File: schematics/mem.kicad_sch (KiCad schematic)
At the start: 6 parts, among them SW2 SW_DIP_x03, U8 SST39SF010A-70-4C-PHE, U9 AS7C256C-15PCN

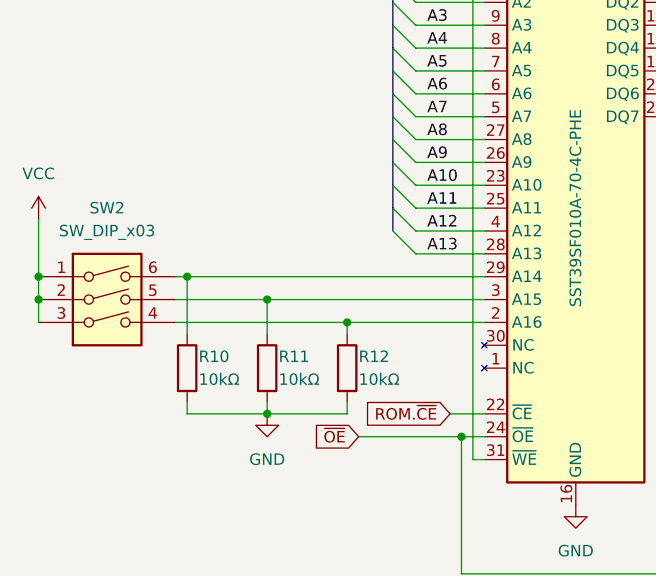
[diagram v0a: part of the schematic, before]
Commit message: Address decoder pld file and no-VIA keyboard schematic and pld file.
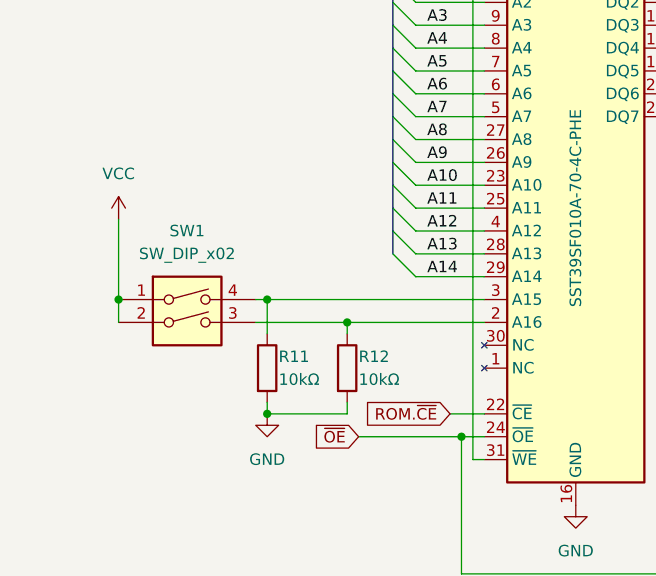
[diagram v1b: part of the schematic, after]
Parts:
- removed R10: 10kΩ, symbol Device:R
- removed SW2: SW_DIP_x03, symbol Switch:SW_DIP_x03
- added SW1: SW_DIP_x02, symbol Switch:SW_DIP_x02
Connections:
- net A14: now also U8.29 (A14)
- net VCC: now also SW1.1, SW1.2
- net at R12.1, U8.2 (A16): now also SW1.3
- net at R11.1, U8.3 (A15): now also SW1.4

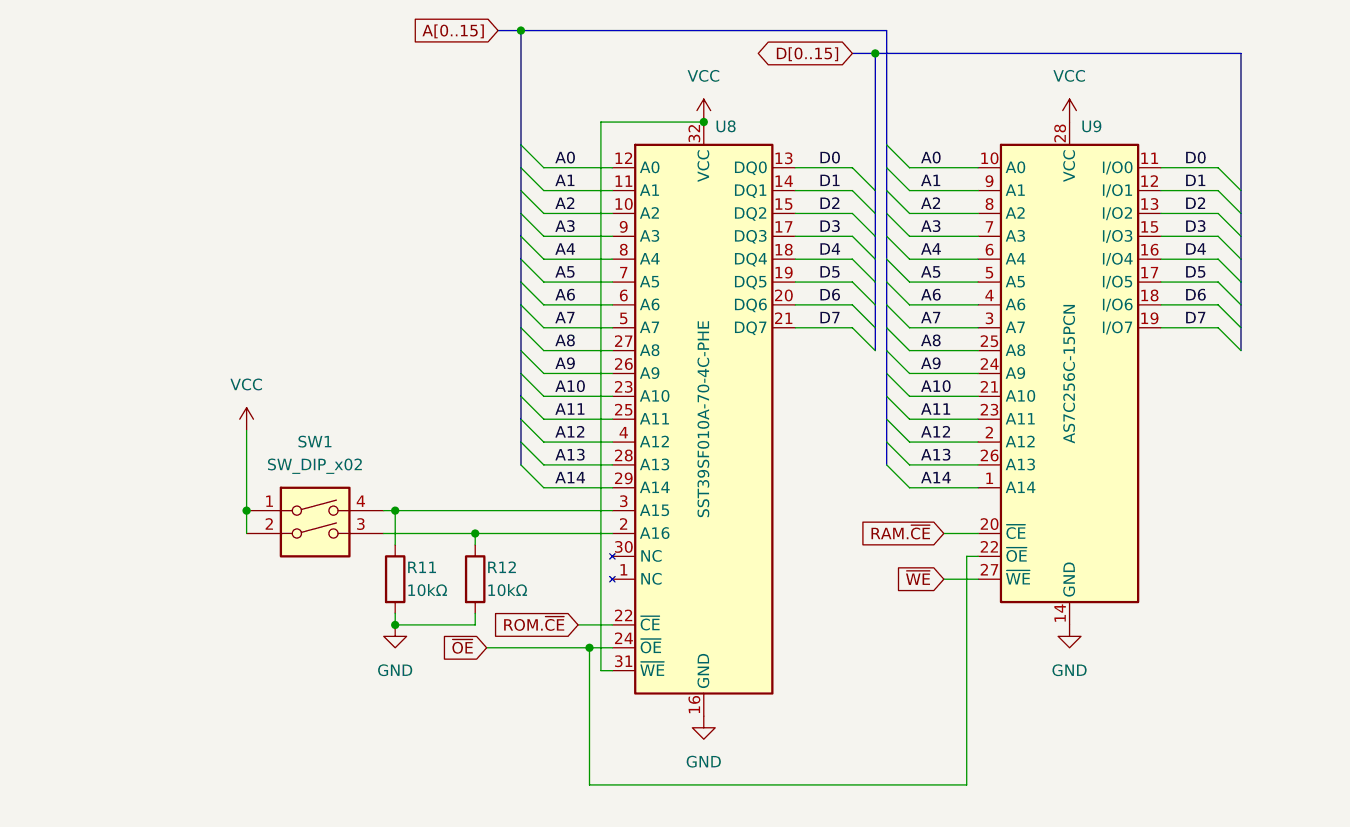
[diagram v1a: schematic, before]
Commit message: PLD files and schematics for address decoder, device selector, keyboard controller, lcd controller, banked memory, and bootloader.
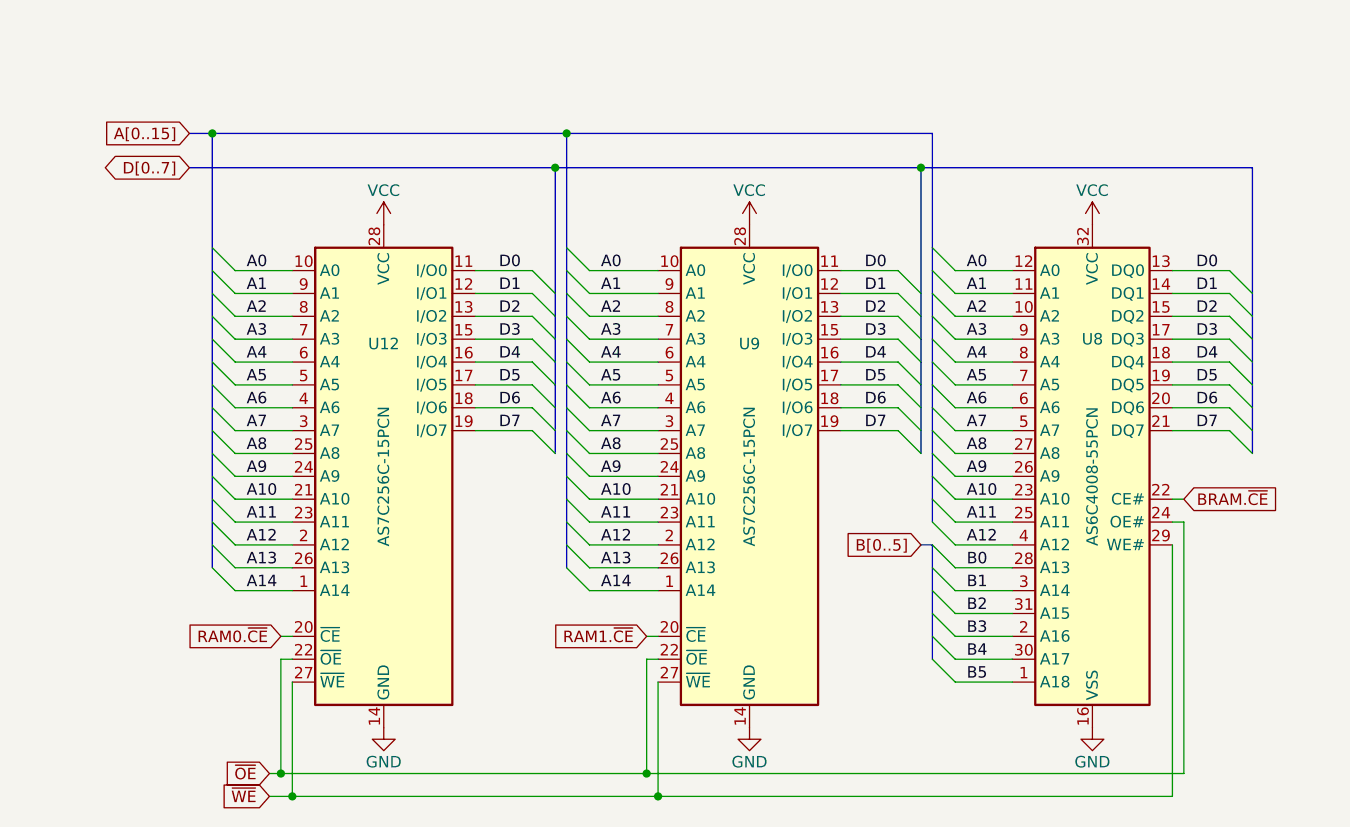
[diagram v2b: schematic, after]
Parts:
- removed R11, R12: 10kΩ, symbol Device:R
- removed SW1: SW_DIP_x02, symbol Switch:SW_DIP_x02
- removed U8: SST39SF010A-70-4C-PHE, symbol Memory_Flash:SST39SF010
- added U12: AS7C256C-15PCN, Package_DIP:DIP-28_W7.62mm, symbol Memory_RAM:KM62256CLP
- added U8: AS6C4008-55PCN, Package_DIP:DIP-32_W15.24mm, symbol Memory_RAM:AS6C4008-55PCN
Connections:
- net A0: now also U12.10 (A0), U8.12 (A0)
- net A1: now also U12.9 (A1), U8.11 (A1)
- net A10: now also U12.21 (A10), U8.23 (A10)
- net A11: now also U12.23 (A11), U8.25 (A11)
- net A12: now also U12.2 (A12), U8.4 (A12)
- net A13: now also U12.26 (A13)
- net A14: now also U12.1 (A14)
- net A2: now also U12.8 (A2), U8.10 (A2)
- net A3: now also U12.7 (A3), U8.9 (A3)
- net A4: now also U12.6 (A4), U8.8 (A4)
- net A5: now also U12.5 (A5), U8.7 (A5)
- net A6: now also U12.4 (A6), U8.6 (A6)
- net A7: now also U12.3 (A7), U8.5 (A7)
- net A8: now also U12.25 (A8), U8.27 (A8)
- net A9: now also U12.24 (A9), U8.26 (A9)
- net D0: now also U12.11 (I/O0), U8.13 (DQ0)
- net D1: now also U12.12 (I/O1), U8.14 (DQ1)
- net D2: now also U12.13 (I/O2), U8.15 (DQ2)
- net D3: now also U12.15 (I/O3), U8.17 (DQ3)
- net D4: now also U12.16 (I/O4), U8.18 (DQ4)
- net D5: now also U12.17 (I/O5), U8.19 (DQ5)
- net D6: now also U12.18 (I/O6), U8.20 (DQ6)
- net D7: now also U12.19 (I/O7), U8.21 (DQ7)
- net GND: now also U12.14 (GND), U8.16 (VSS)
- net VCC: now also U12.28 (VCC), U8.32 (VCC)
- net ~{OE}: now also U12.22 (~{OE}), U8.24 (OE#)
- net ~{WE}: now also U12.27 (~{WE}), U8.29 (WE#)
- net RAM.~{CE} renamed RAM1.~{CE}
- new net B0: U8.28 (A13)
- new net B1: U8.3 (A14)
- new net B2: U8.31 (A15)
- new net B3: U8.2 (A16)
- new net B4: U8.30 (A17)
- new net B5: U8.1 (A18)
- new net BRAM.~{CE}: U8.22 (CE#)
- new net RAM0.~{CE}: U12.20 (~{CE})
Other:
- moved on the sheet: U9

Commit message: updating schematics as I wire the board
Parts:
- renumbered U9 to U13, U8 to U14
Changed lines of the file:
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@@
 		(in_pos_files yes)
 		(dnp no)
-		(property "Reference" "#PWR019"
+		(property "Reference" "#PWR026"
 			(at 100.33 138.43 0)
 			(hide yes)
@@
 			(project "bv6502_hw"
 				(path "/94c72abe-aaa5-49aa-8ab7-5d3e7cbc10be/e0ef0165-61c4-4081-b725-ec037a3db6b2"
-					(reference "#PWR019")
+					(reference "#PWR026")
 					(unit 1)
 				)
@@
 		(in_pos_files yes)
 		(dnp no)
-		(property "Reference" "#PWR018"
+		(property "Reference" "#PWR025"
 			(at 100.33 80.01 0)
 			(hide yes)
@@
 			(project "bv6502_hw"
 				(path "/94c72abe-aaa5-49aa-8ab7-5d3e7cbc10be/e0ef0165-61c4-4081-b725-ec037a3db6b2"
-					(reference "#PWR018")
+					(reference "#PWR025")
 					(unit 1)
 				)
@@
 		(in_pos_files yes)
 		(dnp no)
-		(property "Reference" "U9"
+		(property "Reference" "U13"
 			(at 140.97 90.17 0)
 			(show_name no)
@@
 			(project "bv6502_hw"
 				(path "/94c72abe-aaa5-49aa-8ab7-5d3e7cbc10be/e0ef0165-61c4-4081-b725-ec037a3db6b2"
-					(reference "U9")
+					(reference "U13")
 					(unit 1)
 				)
@@
 		(dnp no)
 		(fields_autoplaced yes)
-		(property "Reference" "U8"
+		(property "Reference" "U14"
 			(at 179.07 88.9 0)
 			(show_name no)
@@
 			(project "bv6502_hw"
 				(path "/94c72abe-aaa5-49aa-8ab7-5d3e7cbc10be/e0ef0165-61c4-4081-b725-ec037a3db6b2"
-					(reference "U8")
+					(reference "U14")
 					(unit 1)
 				)
@@
 		(in_pos_files yes)
 		(dnp no)
-		(property "Reference" "#PWR020"
+		(property "Reference" "#PWR027"
 			(at 140.97 80.01 0)
 			(hide yes)
@@
 			(project "bv6502_hw"
 				(path "/94c72abe-aaa5-49aa-8ab7-5d3e7cbc10be/e0ef0165-61c4-4081-b725-ec037a3db6b2"
-					(reference "#PWR020")
+					(reference "#PWR027")
 					(unit 1)
 				)
@@
 		(in_pos_files yes)
 		(dnp no)
-		(property "Reference" "#PWR021"
+		(property "Reference" "#PWR028"
 			(at 140.97 138.43 0)
 			(hide yes)
@@
 			(project "bv6502_hw"
 				(path "/94c72abe-aaa5-49aa-8ab7-5d3e7cbc10be/e0ef0165-61c4-4081-b725-ec037a3db6b2"
-					(reference "#PWR021")
+					(reference "#PWR028")
 					(unit 1)
 				)
@@
 		(in_pos_files yes)
 		(dnp no)
-		(property "Reference" "#PWR028"
+		(property "Reference" "#PWR030"
 			(at 179.07 138.43 0)
 			(hide yes)
@@
 			(project "bv6502_hw"
 				(path "/94c72abe-aaa5-49aa-8ab7-5d3e7cbc10be/e0ef0165-61c4-4081-b725-ec037a3db6b2"
-					(reference "#PWR028")
+					(reference "#PWR030")
 					(unit 1)
 				)
@@
 		(in_pos_files yes)
 		(dnp no)
-		(property "Reference" "#PWR027"
+		(property "Reference" "#PWR029"
 			(at 179.07 80.01 0)
 			(hide yes)
@@
 			(project "bv6502_hw"
 				(path "/94c72abe-aaa5-49aa-8ab7-5d3e7cbc10be/e0ef0165-61c4-4081-b725-ec037a3db6b2"
-					(reference "#PWR027")
+					(reference "#PWR029")
 					(unit 1)
 				)

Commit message: added some picorom and pld writing stuff to makefiles
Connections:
- net RAM0.~{CE}: now also U13.20 (~{CE}); no longer U12.20 (~{CE})
- net RAM1.~{CE}: now also U12.20 (~{CE}); no longer U13.20 (~{CE})
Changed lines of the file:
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@@
-		)
-	)
-	(wire
-		(pts
-			(xy 129.54 121.92) (xy 130.81 121.92)
-		)
-		(stroke
-			(width 0)
-			(type default)
 		)
 	)
@@
 		(pts
 			(xy 163.83 124.46) (xy 170.18 124.46)
-		)
-		(stroke
-			(width 0)
-			(type default)
-		)
-	)
-	(wire
-		(pts
-			(xy 88.9 121.92) (xy 90.17 121.92)
 		)
 		(stroke
@@
 	(global_label "RAM0.~{CE}"
 		(shape input)
-		(at 88.9 121.92 180)
+		(at 130.81 121.92 180)
 		(fields_autoplaced yes)
 		(effects
@@
 		)
 		(property "Intersheetrefs" "${INTERSHEET_REFS}"
-			(at 77.8715 121.92 0)
+			(at 119.7815 121.92 0)
 			(hide yes)
 			(show_name no)
@@
 	(global_label "RAM1.~{CE}"
 		(shape input)
-		(at 129.54 121.92 180)
+		(at 90.17 121.92 180)
 		(fields_autoplaced yes)
 		(effects
@@
 		)
 		(property "Intersheetrefs" "${INTERSHEET_REFS}"
-			(at 118.5115 121.92 0)
+			(at 79.1415 121.92 0)
 			(hide yes)
 			(show_name no)

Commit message: clock improvements
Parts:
- added R45, R46, R47: 100K, symbol Device:R
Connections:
- net RAM0.~{CE}: now also R47.2
- net RAM1.~{CE}: now also R46.2
- net VCC: now also R45.1, R46.1, R47.1
- net ~{WE}: now also R45.2
